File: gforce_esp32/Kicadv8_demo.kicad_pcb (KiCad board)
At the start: 8 copper layers, 160 x 160 mm, 64 parts, among them J1 USB_C_Receptacle, SW1 TL3215AF160BQ, SW2 TL3215AF160RQ, U1 ESP32-S3-MINI-1U, U2 AP2112K-3.3, U3 LIS3DH

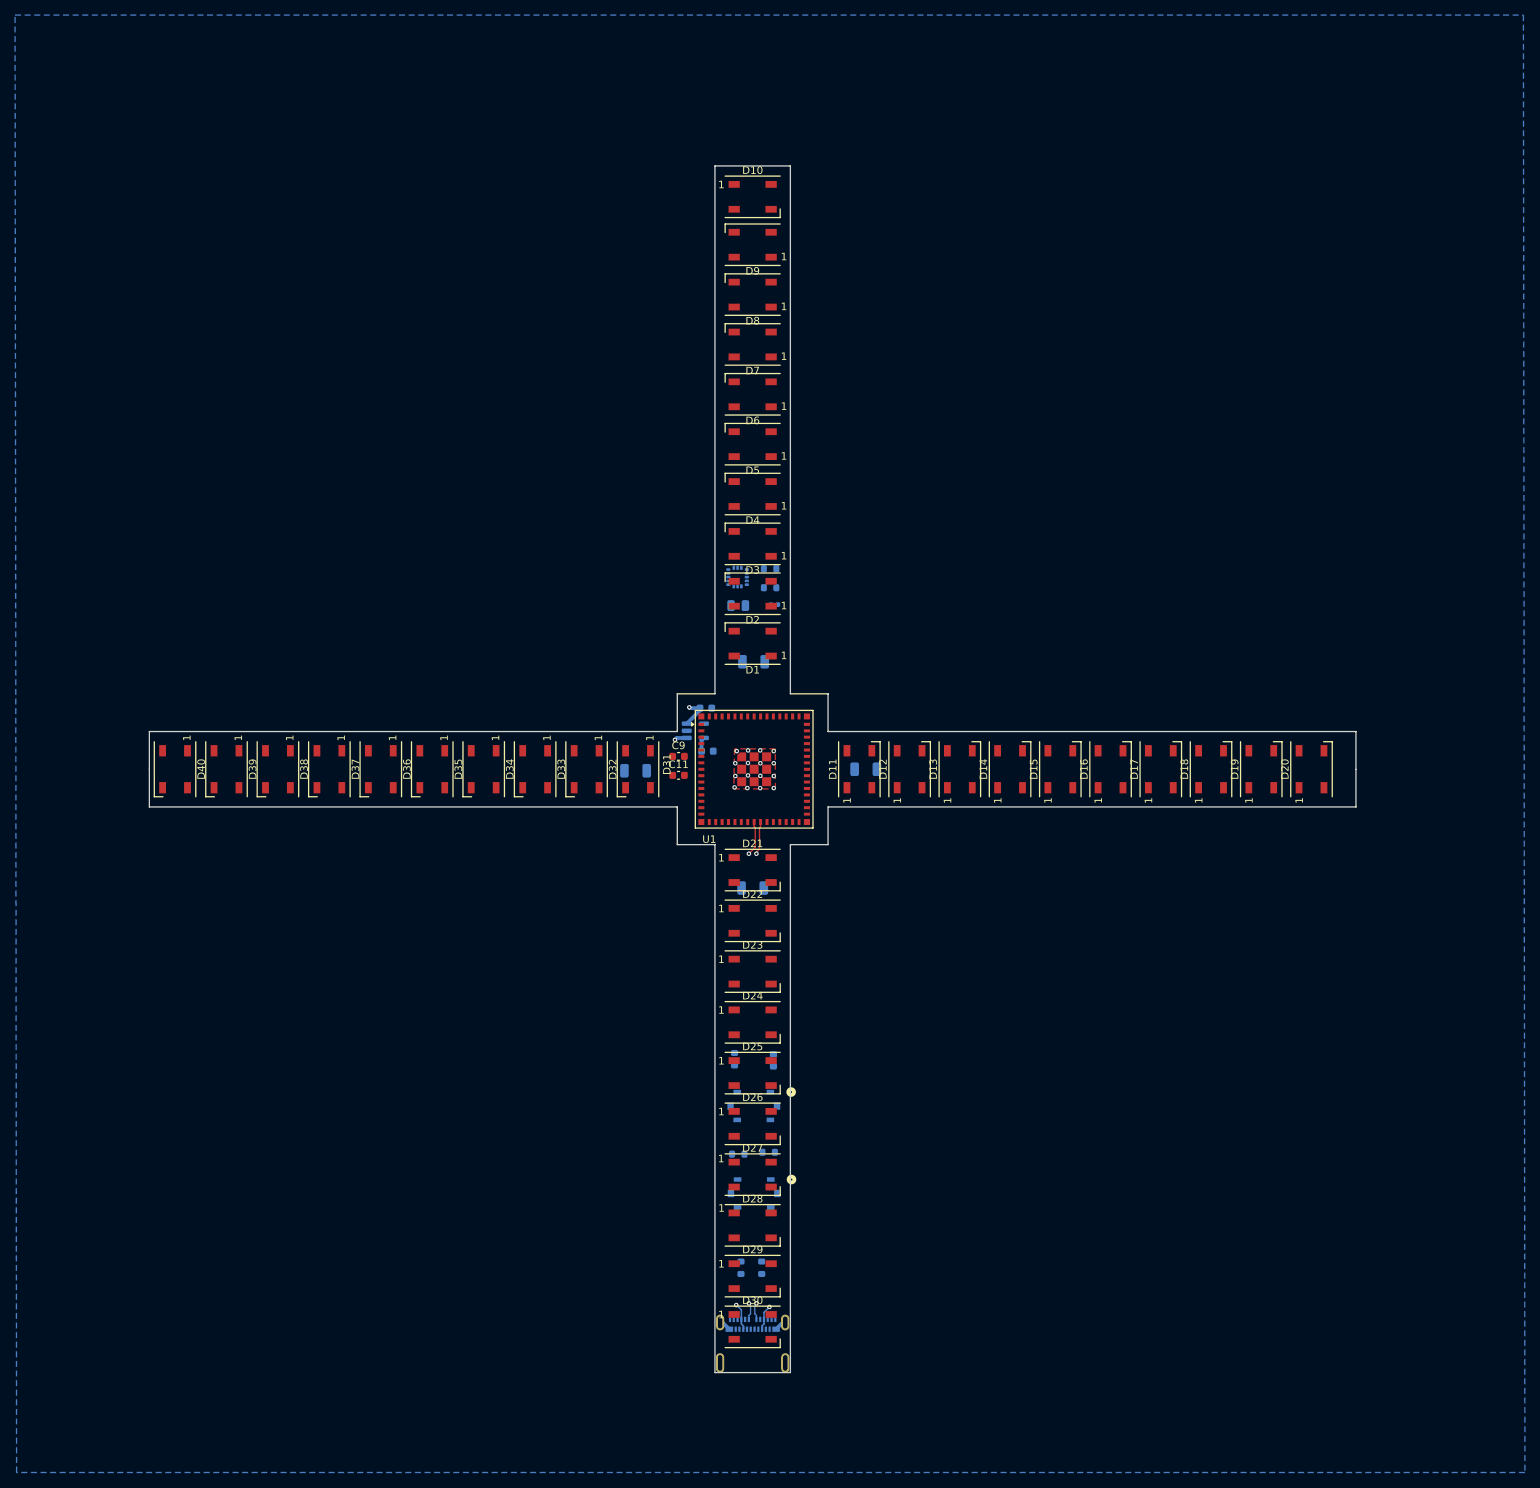
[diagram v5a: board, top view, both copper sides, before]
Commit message: most important traces started to route
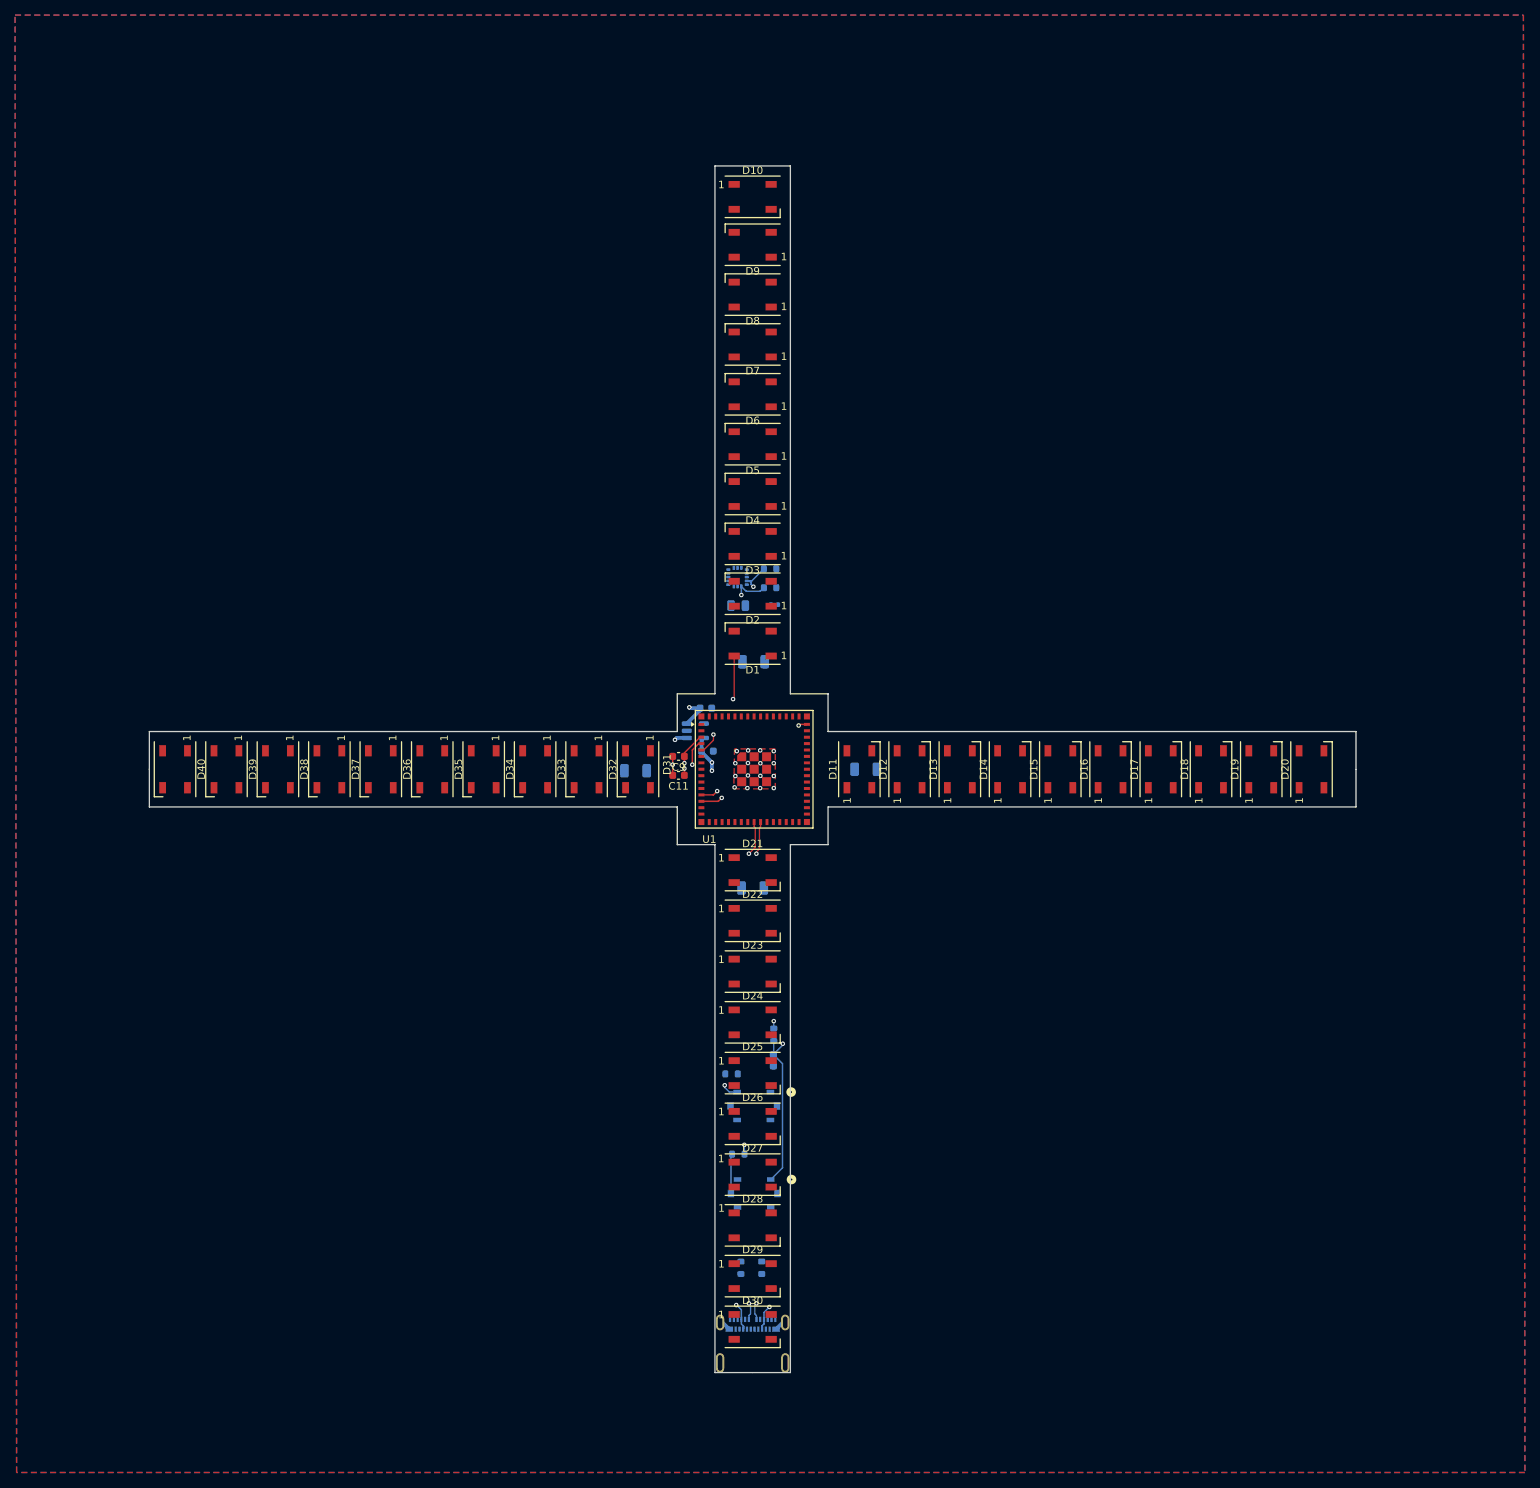
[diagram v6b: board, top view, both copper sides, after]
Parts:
- moved R5 11.5 mm to (135.0, 160.4)
- moved R6 6.13 mm to (140.6, 155.2)
- turned C11 to 180 degrees
- turned C9 to 180 degrees
- turned R3 to 0 degrees
- turned R4 to 0 degrees
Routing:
- net /RESET: track 0.00 -> 65.7 mm, vias 0 -> 2
- net /BOOT_A: track 0.00 -> 51.1 mm, vias 0 -> 2
- net /SCL: track 0.00 -> 36.9 mm, vias 0 -> 2
- net /SDA: track 0.00 -> 34.2 mm, vias 0 -> 2
- net /NEOPXL: track 0.00 -> 14.4 mm, vias 0 -> 2
- net +3V3: track 1.88 -> 13.4 mm, vias 0 -> 6
- net Net-(R7-Pad2): track 0.00 -> 5.28 mm
- net GND: track 3.04 -> 5.55 mm, vias 16 -> 17
- added copper zone on In4.Cu, net +3V3
- added copper zone on In6.Cu, net GND

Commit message: all routing done
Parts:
- moved R1 1.92 mm to (140.5, 187.3), turned to 0 degrees
- moved R2 1.33 mm to (135.5, 187.2), turned to 0 degrees
- moved C2 0.95 mm to (137.8, 136.7)
- turned D10 to 180 degrees
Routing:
- net Net-(D30-DOUT): track 0.00 -> 84.0 mm, vias 0 -> 2
- net Net-(D10-DOUT): track 0.00 -> 81.4 mm
- net Net-(D20-DOUT): track 0.00 -> 78.4 mm
- net +5V: track 12.9 -> 82.3 mm, vias 4 -> 45
- net +3V3: track 13.4 -> 28.1 mm, vias 6 -> 10
- net GND: track 5.55 -> 13.9 mm, vias 17 -> 20
- net Net-(J1-CC2): track 0.00 -> 8.12 mm, vias 0 -> 3
- net Net-(D26-DOUT): track 0.00 -> 6.70 mm
- net Net-(D29-DOUT): track 0.00 -> 6.58 mm
- net Net-(D39-DOUT): track 0.00 -> 6.36 mm
- net Net-(D38-DOUT): track 0.00 -> 6.36 mm
- net Net-(D37-DOUT): track 0.00 -> 6.36 mm
- net Net-(D33-DOUT): track 0.00 -> 6.36 mm
- net Net-(D32-DOUT): track 0.00 -> 6.36 mm
- net Net-(D31-DOUT): track 0.00 -> 6.36 mm
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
